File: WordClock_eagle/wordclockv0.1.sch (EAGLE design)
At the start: 9 parts, among them Q1 8MHz, Q2 32.768kHz

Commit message: Corrected spelling error. Worked on schematic.
Spelling was bugging me. Had to get this out:disappointed_relieved:
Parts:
- added IC1: TLC5925, Treiberplatine:TLC5925
- added R2: 1k, rcl:R-EU_M1206
- U$1: value STM32F030CT6TR -> STM32F030RCT6TR; device STM32F030CT6TR:STM32F030CT6TR -> STM32F030CT6TR:STM32F030RCT6TR
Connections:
- new net !OE: IC1.!OE, U$1.PA3
- new net N$5: IC1.SDI, U$1.PA0
- new net N$6: IC1.CLK, U$1.PA1
- new net N$7: IC1.LE, U$1.PA2
- new net N$9: IC1.R-EXT, R2.1
- net GND: now also IC1.GND, R2.2
- net VDD: now also IC1.VDD

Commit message: Changed the crystal
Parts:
- Q1, Q2: device crystal:CRYSTALHC33U-V -> crystal:CRYSTALTC26V
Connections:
- net N$1: now also Q1.1; no longer Q1.2
- net N$2: now also Q1.2; no longer Q1.1
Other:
- moved on the sheet: C1, C2, C3, C4, IC1, J1, Q1, Q2, R1, R2

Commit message: Started the board. Still a lot of problems. not finished
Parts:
- added C5, C6: 100n, rcl:C-EUC1206
- added C7: 10uF, rcl:CPOL-EUE2-5
- added IC3: REG1117, burr-brown:REG1117
- C1, C2: value TBD -> 18pF; device rcl:C-EU025-025X050 -> rcl:C-EUC1206
- C3, C4: value TBD -> 12,5pF; device rcl:C-EU025-025X050 -> rcl:C-EUC1206
- Q1: device crystal:CRYSTALTC26V -> crystal:CRYSTALHC49U-V
- U$1: device STM32F030CT6TR:STM32F030RCT6TR -> STM32F030RCT6TR:STM32F030RCT6TR
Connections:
- removed net N$6: IC1.CLK, U$1.PA1
- removed net N$7: IC1.LE, U$1.PA2
- new net CLK: IC1.CLK, U$1.PA5
- new net LE: IC1.LE, U$1.PA6
- new net SDI: IC1.SDI, U$1.PA4
- net !OE: now also U$1.PA7; no longer U$1.PA3
- net GND: now also C5.2, C6.2, C7.-, IC3.GND
- net N$5: now also C5.1, IC3.VIN, J1.1; no longer IC1.SDI, U$1.PA0
- net VDD: now also C6.1, C7.+, IC3.VOUT; no longer J1.1
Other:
- moved on the sheet: J1

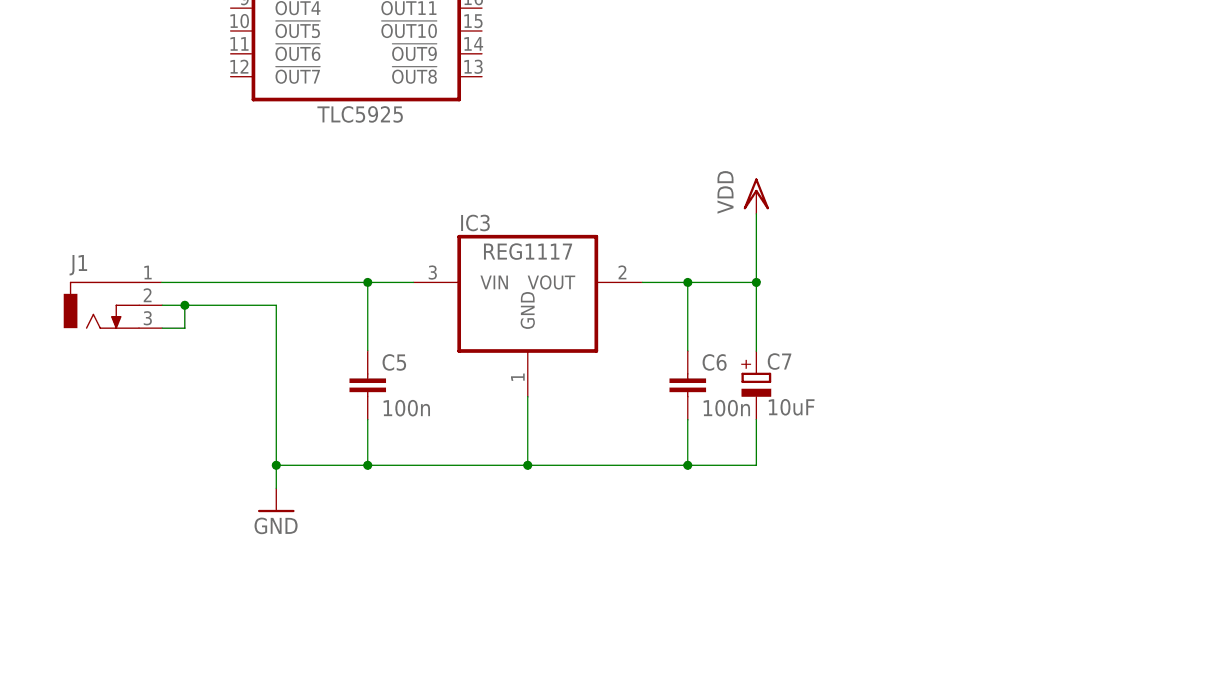
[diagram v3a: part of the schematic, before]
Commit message: schematic changes. deleted brd. lbr changes
board was deleted because i added a switching regulator and i'd need to rework the whole thing anyway. no point in keeping it. :imp:
I also added devices for the regulator and the inductor i need to the lbr.
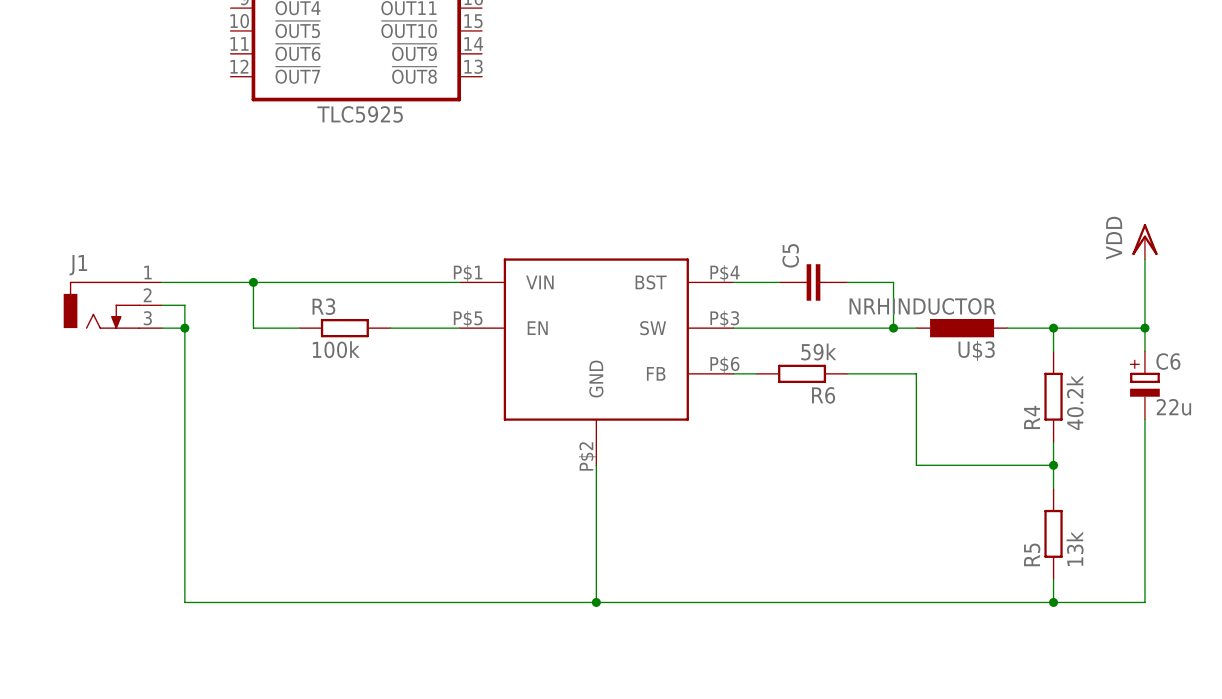
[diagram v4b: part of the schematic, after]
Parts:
- removed C7: 10uF, rcl:CPOL-EUE2-5
- removed IC3: REG1117, burr-brown:REG1117
- added R3: 100k, rcl:R-EU_M1206
- added R4: 40.2k, rcl:R-EU_M1206
- added R5: 13k, rcl:R-EU_M1206
- added R6: 59k, rcl:R-EU_M1206
- added U$2: AP65111A, STM32F030RCT6TR:AP65111A
- added U$3: NRHINDUCTOR, STM32F030RCT6TR:NRHINDUCTOR
- C5: value 100n -> (none)
- C6: value 100n -> 22u; device rcl:C-EUC1206 -> rcl:CPOL-EU140CLH-1010
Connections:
- new net N$10: C5.2, U$2.SW, U$3.1
- new net N$11: R6.2, U$2.FB
- new net N$12: R4.1, R5.2, R6.1
- new net N$6: C5.1, U$2.BST
- new net N$7: R3.2, U$2.EN
- new net N$8: C6.-, J1.2, J1.3, R5.1, U$2.GND
- net GND: no longer C5.2, C6.2, C7.-, IC3.GND, J1.2, J1.3
- net N$5: now also R3.1, U$2.VIN; no longer C5.1, IC3.VIN
- net VDD: now also C6.+, R4.2, U$3.2; no longer C6.1, C7.+, IC3.VOUT
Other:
- moved on the sheet: C5

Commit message: Finished schematic for now. Starting on board
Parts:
- added JP1: (no value), pinhead:PINHD-1X11
- added JP2: (no value), pinhead:PINHD-1X10
- added R10, R11, R12, R13, R14, R15, R16, R7, R8, R9: 1k, rcl:R-EU_M1206
- added S1, S2: DTE6K, switch-misc:DTE6K
- added U1, U2, U3, U4, U5: MBT3906DW1T1G, STM32F030RCT6TR:MBT3906DW1T1G
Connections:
- new net COL1: JP2.1, U4T1.C
- new net COL10: JP2.10, U5T2.C
- new net COL2: JP2.2, U4T2.C
- new net COL3: JP2.3, U1T1.C
- new net COL4: JP2.4, U1T2.C
- new net COL5: JP2.5, U2T1.C
- new net COL6: JP2.6, U2T2.C
- new net COL7: JP2.7, U3T1.C
- new net COL8: JP2.8, U3T2.C
- new net COL9: JP2.9, U5T1.C
- new net LCOL1: R7.2, U$1.PB12
- new net LCOL10: R16.2, U$1.PA9
- new net LCOL2: R8.2, U$1.PB13
- new net LCOL3: R9.2, U$1.PB14
- new net LCOL4: R10.2, U$1.PB15
- new net LCOL5: R11.2, U$1.PC6
- new net LCOL6: R12.2, U$1.PC7
- new net LCOL7: R13.2, U$1.PC8
- new net LCOL8: R14.2, U$1.PC9
- new net LCOL9: R15.2, U$1.PA8
- new net N$13: R7.1, U4T1.B
- new net N$14: R8.1, U4T2.B
- new net N$15: IC1.!OUT5, JP1.11
- new net N$16: S1.P, U$1.PC0
- new net N$17: R9.1, U1T1.B
- new net N$18: R10.1, U1T2.B
- new net N$20: S2.P, U$1.PC1
- new net N$21: R11.1, U2T1.B
- new net N$22: R12.1, U2T2.B
- new net N$24: IC1.!OUT15, JP1.1
- new net N$25: IC1.!OUT14, JP1.2
- new net N$26: IC1.!OUT13, JP1.3
- new net N$27: IC1.!OUT12, JP1.4
- new net N$28: IC1.!OUT11, JP1.5
- new net N$29: IC1.!OUT10, JP1.6
- new net N$30: IC1.!OUT9, JP1.7
- new net N$31: IC1.!OUT8, JP1.8
- new net N$32: IC1.!OUT7, JP1.9
- new net N$33: IC1.!OUT6, JP1.10
- new net N$35: R13.1, U3T1.B
- new net N$36: R14.1, U3T2.B
- new net N$39: R15.1, U5T1.B
- new net N$40: R16.1, U5T2.B
- net GND: now also S1.S, S2.S
- net VDD: now also U1T1.E, U1T2.E, U2T1.E, U2T2.E, U3T1.E, U3T2.E, U4T1.E, U4T2.E, U5T1.E, U5T2.E

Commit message: Did the board. Rough draft without consideration for manufacturing
Fabricating this thing is going to be hell :imp:
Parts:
- added JP3: (no value), pinhead:PINHD-1X5
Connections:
- removed net N$8: C6.-, J1.2, J1.3, R5.1, U$2.GND
- net GND: now also C6.-, J1.2, J1.3, JP3.3, R5.1, S1.S@1, S2.S@1, U$2.GND
- net LE: now also U$1.PA4; no longer U$1.PA6
- net N$16: now also S1.P@1
- net N$20: now also S2.P@1
- net NRST: now also JP3.5
- net SDI: now also U$1.PA6; no longer U$1.PA4
- net SWDCLK: now also JP3.2
- net SWDIO: now also JP3.4
- net VDD: now also JP3.1

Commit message: Made a parts list from digikey. Changed some components bc cheaper
Whoa this was a piece of work.
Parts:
- C1, C2, C3, C4: device rcl:C-EUC1206 -> rcl:C-EUC0402
- C5: value (none) -> 1uF; device rcl:C-EUC1206 -> rcl:C-EUC0805
- C6: device rcl:CPOL-EU140CLH-1010 -> rcl:CPOL-EU153CLV-0405
- R1: value 10k -> 100k
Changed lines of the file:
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@@
 <?xml version="1.0" encoding="utf-8"?>
 <!DOCTYPE eagle SYSTEM "eagle.dtd">
-<eagle version="9.2.0">
+<eagle version="9.1.3">
 <drawing>
 <settings>
@@
 <part name="VDD1" library="supply1" library_urn="urn:adsk.eagle:library:371" deviceset="VDD" device=""/>
 <part name="GND1" library="supply1" library_urn="urn:adsk.eagle:library:371" deviceset="GND" device=""/>
-<part name="C1" library="rcl" library_urn="urn:adsk.eagle:library:334" deviceset="C-EU" device="C1206" package3d_urn="urn:adsk.eagle:package:23618/2" value="18pF"/>
-<part name="C2" library="rcl" library_urn="urn:adsk.eagle:library:334" deviceset="C-EU" device="C1206" package3d_urn="urn:adsk.eagle:package:23618/2" value="18pF"/>
-<part name="C3" library="rcl" library_urn="urn:adsk.eagle:library:334" deviceset="C-EU" device="C1206" package3d_urn="urn:adsk.eagle:package:23618/2" value="12,5pF"/>
-<part name="C4" library="rcl" library_urn="urn:adsk.eagle:library:334" deviceset="C-EU" device="C1206" package3d_urn="urn:adsk.eagle:package:23618/2" value="12,5pF"/>
+<part name="C1" library="rcl" deviceset="C-EU" device="C0402" value="18pF"/>
+<part name="C2" library="rcl" library_urn="urn:adsk.eagle:library:334" deviceset="C-EU" device="C0402" value="18pF"/>
+<part name="C3" library="rcl" deviceset="C-EU" device="C0402" value="12,5pF"/>
+<part name="C4" library="rcl" library_urn="urn:adsk.eagle:library:334" deviceset="C-EU" device="C0402" value="12,5pF"/>
 <part name="GND2" library="supply1" library_urn="urn:adsk.eagle:library:371" deviceset="GND" device=""/>
 <part name="GND3" library="supply1" library_urn="urn:adsk.eagle:library:371" deviceset="GND" device=""/>
-<part name="R1" library="rcl" library_urn="urn:adsk.eagle:library:334" deviceset="R-EU_" device="M1206" package3d_urn="urn:adsk.eagle:package:23566/1" value="10k"/>
+<part name="R1" library="rcl" library_urn="urn:adsk.eagle:library:334" deviceset="R-EU_" device="M1206" package3d_urn="urn:adsk.eagle:package:23566/1" value="100k"/>
 <part name="J1" library="con-jack" library_urn="urn:adsk.eagle:library:154" deviceset="DCJ0303" device="" package3d_urn="urn:adsk.eagle:package:7493/1"/>
 <part name="IC1" library="Treiberplatine" deviceset="TLC5925" device=""/>
@@
 <part name="U$2" library="STM32F030RCT6TR" deviceset="AP65111A" device=""/>
 <part name="R3" library="rcl" library_urn="urn:adsk.eagle:library:334" deviceset="R-EU_" device="M1206" package3d_urn="urn:adsk.eagle:package:23566/1" value="100k"/>
-<part name="C5" library="rcl" library_urn="urn:adsk.eagle:library:334" deviceset="C-EU" device="C1206" package3d_urn="urn:adsk.eagle:package:23618/2"/>
+<part name="C5" library="rcl" deviceset="C-EU" device="C0805" value="1uF"/>
 <part name="U$3" library="STM32F030RCT6TR" deviceset="NRHINDUCTOR" device=""/>
-<part name="C6" library="rcl" library_urn="urn:adsk.eagle:library:334" deviceset="CPOL-EU" device="140CLH-1010" package3d_urn="urn:adsk.eagle:package:23391/1" value="22u"/>
+<part name="C6" library="rcl" deviceset="CPOL-EU" device="153CLV-0405" value="22u"/>
 <part name="VDD2" library="supply1" library_urn="urn:adsk.eagle:library:371" deviceset="VDD" device=""/>
 <part name="R4" library="rcl" library_urn="urn:adsk.eagle:library:334" deviceset="R-EU_" device="M1206" package3d_urn="urn:adsk.eagle:package:23566/1" value="40.2k"/>

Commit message: Small changes to schematic and pcb
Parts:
- S1, S2: value DTE6K -> (none); device switch-misc:DTE6K -> switch-omron:10-XX
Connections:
- net GND: now also S1.S1, S2.S1; no longer S1.S@1, S2.S@1
- net N$16: now also S1.P1; no longer S1.P@1
- net N$20: now also S2.P1; no longer S2.P@1
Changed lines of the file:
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@@
 <?xml version="1.0" encoding="utf-8"?>
 <!DOCTYPE eagle SYSTEM "eagle.dtd">
-<eagle version="9.1.3">
+<eagle version="9.2.0">
 <drawing>
 <settings>
@@
 <part name="R15" library="rcl" library_urn="urn:adsk.eagle:library:334" deviceset="R-EU_" device="M1206" package3d_urn="urn:adsk.eagle:package:23566/1" value="1k"/>
 <part name="R16" library="rcl" library_urn="urn:adsk.eagle:library:334" deviceset="R-EU_" device="M1206" package3d_urn="urn:adsk.eagle:package:23566/1" value="1k"/>
-<part name="S1" library="switch-misc" library_urn="urn:adsk.eagle:library:376" deviceset="DT" device="E6K" package3d_urn="urn:adsk.eagle:package:27433/1"/>
-<part name="S2" library="switch-misc" library_urn="urn:adsk.eagle:library:376" deviceset="DT" device="E6K" package3d_urn="urn:adsk.eagle:package:27433/1"/>
+<part name="S1" library="switch-omron" library_urn="urn:adsk.eagle:library:377" deviceset="10-XX" device="" package3d_urn="urn:adsk.eagle:package:27496/1"/>
+<part name="S2" library="switch-omron" library_urn="urn:adsk.eagle:library:377" deviceset="10-XX" device="" package3d_urn="urn:adsk.eagle:package:27496/1"/>
 <part name="GND4" library="supply1" library_urn="urn:adsk.eagle:library:371" deviceset="GND" device=""/>
 <part name="JP3" library="pinhead" library_urn="urn:adsk.eagle:library:325" deviceset="PINHD-1X5" device="" package3d_urn="urn:adsk.eagle:package:22469/2"/>
@@
 <junction x="106.68" y="137.16"/>
 <junction x="154.94" y="124.46"/>
-<pinref part="S2" gate="1" pin="S@1"/>
+<pinref part="S2" gate="1" pin="S1"/>
 <wire x1="109.22" y1="129.54" x2="109.22" y2="132.08" width="0.1524" layer="91"/>
 <wire x1="109.22" y1="132.08" x2="106.68" y2="132.08" width="0.1524" layer="91"/>
 <junction x="106.68" y="132.08"/>
-<pinref part="S1" gate="1" pin="S@1"/>
+<pinref part="S1" gate="1" pin="S1"/>
 <wire x1="96.52" y1="129.54" x2="96.52" y2="132.08" width="0.1524" layer="91"/>
 <wire x1="96.52" y1="132.08" x2="93.98" y2="132.08" width="0.1524" layer="91"/>
@@
 <pinref part="U$1" gate="G$1" pin="PC0"/>
 <wire x1="99.06" y1="109.22" x2="99.06" y2="104.14" width="0.1524" layer="91"/>
-<pinref part="S1" gate="1" pin="P@1"/>
+<pinref part="S1" gate="1" pin="P1"/>
 <wire x1="96.52" y1="119.38" x2="96.52" y2="116.84" width="0.1524" layer="91"/>
 <wire x1="96.52" y1="116.84" x2="93.98" y2="116.84" width="0.1524" layer="91"/>
@@
 <pinref part="U$1" gate="G$1" pin="PC1"/>
 <wire x1="101.6" y1="109.22" x2="101.6" y2="104.14" width="0.1524" layer="91"/>
-<pinref part="S2" gate="1" pin="P@1"/>
+<pinref part="S2" gate="1" pin="P1"/>
 <wire x1="109.22" y1="119.38" x2="109.22" y2="116.84" width="0.1524" layer="91"/>
 <wire x1="109.22" y1="116.84" x2="106.68" y2="116.84" width="0.1524" layer="91"/>
